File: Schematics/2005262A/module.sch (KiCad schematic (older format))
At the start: 0 parts

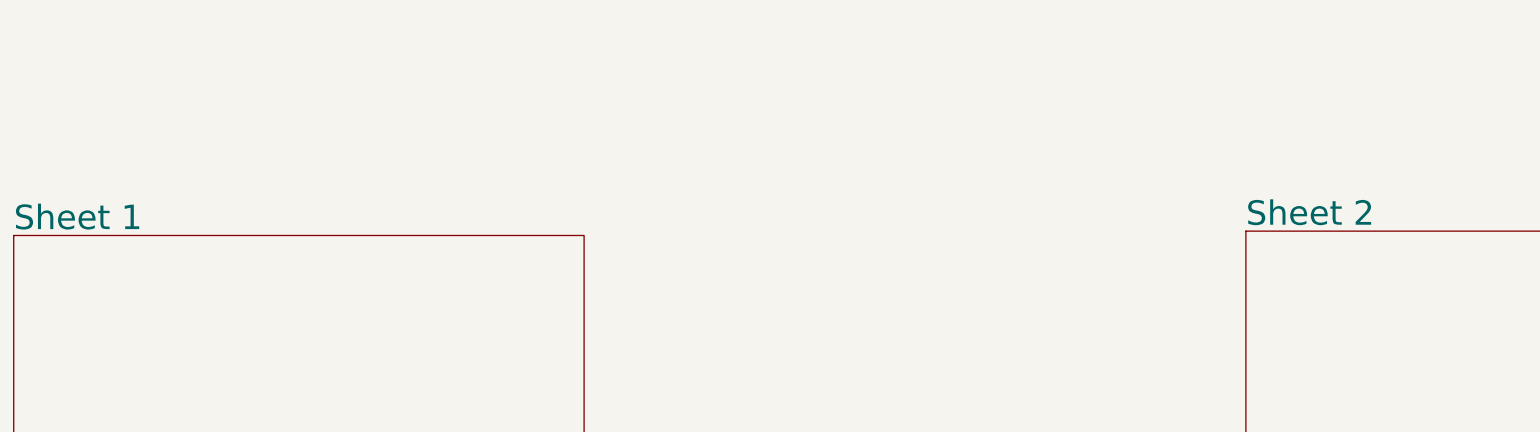
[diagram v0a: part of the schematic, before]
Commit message: Cross-checked/corrected connector captions on module A4 CAD vs Mike's pin database.
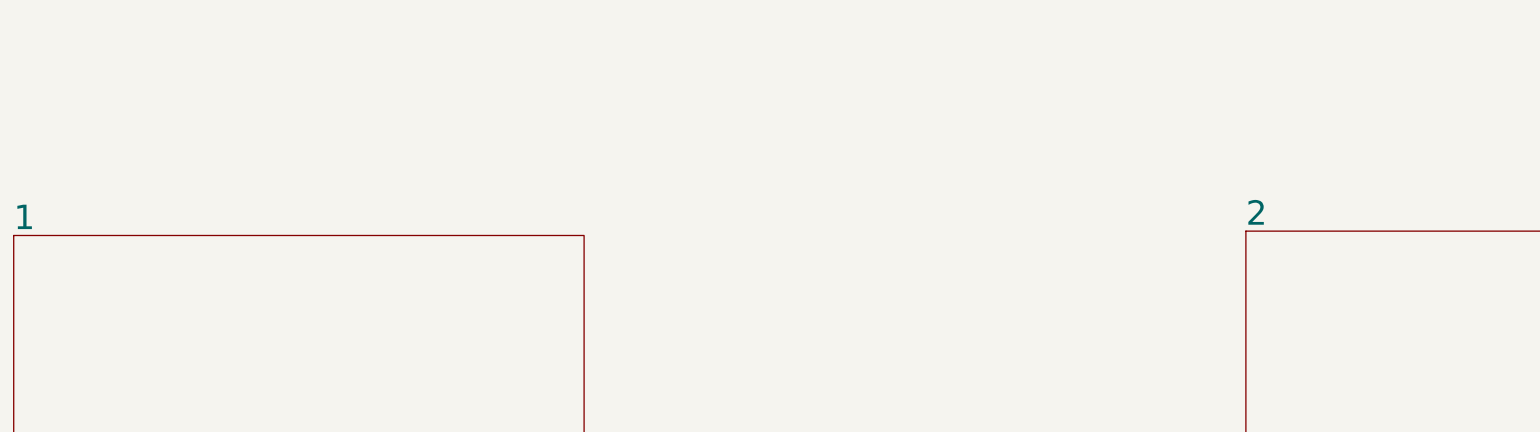
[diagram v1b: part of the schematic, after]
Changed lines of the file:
@@
 S 17375 14775 3275 4875
 U 5B86CFFC
-F0 "Sheet 1" 140
+F0 "1" 140
 F1 "2005262A-p1of2.sch" 140
 F2 "FAP" U R 20650 16500 140
@@
 S 24450 14750 3300 4925
 U 5B86D026
-F0 "Sheet 2" 140
+F0 "2" 140
 F1 "2005262A-p2of2.sch" 140
 F2 "FAP" U L 24450 16500 140
